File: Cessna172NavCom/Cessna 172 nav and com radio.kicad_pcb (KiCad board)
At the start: 2 copper layers, 180 x 48 mm, 54 parts, among them J1 Conn_02x10_Odd_Even, J2 USB_B_Micro, J3 EN11-HSM1BF20, J4 EN11-HSM1BF20, J5 EN11-HSM1BF20, J6 Conn_01x05, SW1 SW_Push, SW2 SW_Push, SW3 SW_Push, U1 MAX7219 COM standby, U2 3651A, U3 MAX7219 COM standby, U4 3651A, U5 MAX7219 COM standby, U6 3651A, U7 MAX7219 COM standby, U8 3651A

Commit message: Updated trace width for +5V and GND
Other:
- net class +5V: trace_width 1.016 -> 0.4
- net class GND: trace_width 1.016 -> 0.4

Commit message: Mostly laid out
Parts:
- added C12: 0.1uF, Capacitor_SMD:C_0805_2012Metric_Pad1.15x1.40mm_HandSolder, F.Cu at (195.0, 177.0)
- added C13: 0.1uF, Capacitor_SMD:C_0805_2012Metric_Pad1.15x1.40mm_HandSolder, F.Cu at (210.0, 172.0)
- added C14: 0.1uF, Capacitor_SMD:C_0805_2012Metric_Pad1.15x1.40mm_HandSolder, F.Cu at (205.0, 177.0)
- added C15: 0.1uF, Capacitor_SMD:C_0805_2012Metric_Pad1.15x1.40mm_HandSolder, F.Cu at (210.0, 168.0)
- added C16: 0.1uf, Capacitor_SMD:C_0805_2012Metric_Pad1.15x1.40mm_HandSolder, B.Cu at (113.0, 121.0)
- added C17: 0.1uf, Capacitor_SMD:C_0805_2012Metric_Pad1.15x1.40mm_HandSolder, B.Cu at (113.0, 101.0)
- added C18: 0.1uf, Capacitor_SMD:C_0805_2012Metric_Pad1.15x1.40mm_HandSolder, B.Cu at (193.0, 121.0)
- added C19: 0.1uf, Capacitor_SMD:C_0805_2012Metric_Pad1.15x1.40mm_HandSolder, B.Cu at (193.0, 101.0)
- added C20: 0.1uf, Capacitor_SMD:C_0805_2012Metric_Pad1.15x1.40mm_HandSolder, B.Cu at (55.0, 125.0)
- added C21: 0.1uf, Capacitor_SMD:C_0805_2012Metric_Pad1.15x1.40mm_HandSolder, B.Cu at (60.0, 104.0)
- added D5: LED, LED_THT:LED_D5.0mm, F.Cu at (203.0, 171.0)
- added D6: LED, LED_THT:LED_D5.0mm, F.Cu at (195.0, 171.0)
- added D7: LED, LED_THT:LED_D5.0mm, F.Cu at (206.0, 163.0)
- added J7: EN11-HSM1BF20, SamacSys_Parts:EN11HSM1BF20, F.Cu at (60.0, 117.0)
- added J8: Conn_02x20_Odd_Even, SamacSys_Parts:SAMTEC-TST-120-01-X-D, B.Cu at (203.0, 77.5)
- added R18: 220k, Resistor_SMD:R_0805_2012Metric_Pad1.15x1.40mm_HandSolder, F.Cu at (213.0, 164.0)
- added R19: 220k, Resistor_SMD:R_0805_2012Metric_Pad1.15x1.40mm_HandSolder, F.Cu at (200.0, 177.0)
- added R20: 220k, Resistor_SMD:R_0805_2012Metric_Pad1.15x1.40mm_HandSolder, F.Cu at (213.0, 161.0)
- added R21: 10k, Resistor_SMD:R_0805_2012Metric_Pad1.15x1.40mm_HandSolder, B.Cu at (108.0, 121.0)
- added R22: 10k, Resistor_SMD:R_0805_2012Metric_Pad1.15x1.40mm_HandSolder, B.Cu at (108.0, 101.0)
- added R23: 10k, Resistor_SMD:R_0805_2012Metric_Pad1.15x1.40mm_HandSolder, B.Cu at (113.0, 117.0)
- added R24: 10k, Resistor_SMD:R_0805_2012Metric_Pad1.15x1.40mm_HandSolder, B.Cu at (113.0, 105.0)
- added R25: 10k, Resistor_SMD:R_0805_2012Metric_Pad1.15x1.40mm_HandSolder, B.Cu at (188.0, 121.0)
- added R26: 10k, Resistor_SMD:R_0805_2012Metric_Pad1.15x1.40mm_HandSolder, B.Cu at (188.0, 101.0)
- added R27: 10k, Resistor_SMD:R_0805_2012Metric_Pad1.15x1.40mm_HandSolder, B.Cu at (193.0, 117.0)
- added R28: 10k, Resistor_SMD:R_0805_2012Metric_Pad1.15x1.40mm_HandSolder, B.Cu at (193.0, 105.0)
- added R29: 10k, Resistor_SMD:R_0805_2012Metric_Pad1.15x1.40mm_HandSolder, B.Cu at (60.0, 125.0)
- added R30: 10k, Resistor_SMD:R_0805_2012Metric_Pad1.15x1.40mm_HandSolder, B.Cu at (55.0, 104.0)
- added R31: 10k, Resistor_SMD:R_0805_2012Metric_Pad1.15x1.40mm_HandSolder, B.Cu at (60.0, 121.0)
- added R32: 10k, Resistor_SMD:R_0805_2012Metric_Pad1.15x1.40mm_HandSolder, B.Cu at (60.0, 108.0)
- added SW4: SW_Push, Button_Switch_THT:SW_PUSH_6mm_H8mm, F.Cu at (184.0, 161.0)
- added SW5: SW_Push, Button_Switch_THT:SW_PUSH_6mm_H8mm, F.Cu at (184.0, 169.0)
- added SW6: SW_Push, Button_Switch_THT:SW_PUSH_6mm_H8mm, F.Cu at (195.0, 161.0)
- added U10: 3651A, Cessna 172 nav and com radio:3651A, F.Cu at (61.0, 91.0)
- added U11: MAX7219 COM standby, Package_SO:SSOP-24_3.9x8.7mm_P0.635mm, B.Cu at (140.0, 91.0)
- added U12: 3651A, Cessna 172 nav and com radio:3651A, F.Cu at (140.0, 91.0)
- added U13: MAX7219 COM standby, Package_SO:SSOP-24_3.9x8.7mm_P0.635mm, B.Cu at (178.0, 91.0)
- added U14: 3651A, Cessna 172 nav and com radio:3651A, F.Cu at (178.0, 91.0)
- added U15: MAX7219 COM standby, Package_SO:SSOP-24_3.9x8.7mm_P0.635mm, B.Cu at (99.0, 91.0)
- added U16: 3651A, Cessna 172 nav and com radio:3651A, F.Cu at (99.0, 91.0)
- added U9: MAX7219 COM standby, Package_SO:SSOP-24_3.9x8.7mm_P0.635mm, B.Cu at (61.0, 91.0)
- J1: value Conn_02x10_Odd_Even -> EN11-HSM1BF20; footprint Connector_PinHeader_2.54mm:PinHeader_2x10_P2.54mm_Vertical -> SamacSys_Parts:EN11HSM1BF20; moved to F.Cu
- J6: value Conn_01x05 -> EN11-HSM1BF20; footprint Connector_PinHeader_2.54mm:PinHeader_1x05_P2.54mm_Vertical -> SamacSys_Parts:EN11HSM1BF20
- moved J6 65.1 mm to (193.0, 113.0), turned to 90 degrees
- moved J1 56.2 mm to (113.5, 113.0), turned to 90 degrees
- moved C1 55.0 mm to (35.0, 101.0)
- moved D1 55.0 mm to (32.0, 96.0)
- moved J2 55.0 mm to (32.8, 109.0)
- moved R2 55.0 mm to (36.0, 96.0)
- moved H2 47.0 mm to (35.0, 120.0)
- moved H4 47.0 mm to (205.0, 120.0)
- moved R1 23.3 mm to (141.0, 56.0)
- moved RV1 23.3 mm to (146.0, 56.0)
- moved D3 4.00 mm to (138.0, 66.0)
- moved R4 4.00 mm to (144.0, 66.0)
- moved SW3 4.00 mm to (125.0, 64.0)
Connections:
- C1 pad 2: GND -> +5V
- C10 pad 1: GND -> +5V
- C11 pad 2: GND -> +5V
- C2 pad 2: GND -> +5V
- C3 pad 2: GND -> +5V
- C4 pad 2: GND -> +5V
- C5 pad 2: GND -> +5V
- C6 pad 1: GND -> +5V
- C7 pad 2: GND -> +5V
- C8 pad 1: GND -> +5V
- C9 pad 2: GND -> +5V
- D1 pad 1: GND -> +5V
- D2 pad 1: GND -> +5V
- D3 pad 1: GND -> +5V
- D4 pad 1: GND -> +5V
- J2 pad 5: GND -> +5V
- J3 pad C1: GND -> +5V
- J3 pad D1: COMM_KHZ_SW -> COMM1_KHZ_SW
- J3 pad E1: GND -> +5V
- J4 pad C1: GND -> +5V
- J4 pad D1: NAV_KHZ_SW -> NAV1_KHZ_SW
- J4 pad E1: GND -> +5V
- J5 pad C1: GND -> +5V
- J5 pad D1: TEST_SW -> TEST1_SW
- J5 pad E1: GND -> +5V
- R11 pad 1: NAV_LEFT -> NAV1_LEFT
- R12 pad 2: NAV_RIGHT -> NAV1_RIGHT
- R15 pad 1: COMM_VOL_LEFT -> COMM1_VOL_LEFT
- R16 pad 2: COMM_VOL_RIGHT -> COMM1_VOL_RIGHT
- R17 pad 2: CHAN_LED -> CHAN1_LED
- R2 pad 1: Net-(D1-Pad2) -> +5V
- R2 pad 2: +5V -> Net-(D1-Pad2)
- R3 pad 2: TEST_LED -> TEST1_LED
- R4 pad 2: IDENT_LED -> IDENT1_LED
- R7 pad 1: COMM_LEFT -> COMM1_LEFT
- R8 pad 2: COMM_RIGHT -> COMM1_RIGHT
- SW1 pad 1: GND -> +5V
- SW1 pad 2: COMM_TX_SW -> COMM1_TX_SW
- SW2 pad 1: GND -> +5V
- SW2 pad 2: NAV_TX_SW -> NAV1_TX_SW
- SW3 pad 1: GND -> +5V
- SW3 pad 2: IDENT_SW -> IDENT1_SW
- U1 pad 4: GND -> +5V
- U1 pad 9: GND -> +5V
- U3 pad 4: GND -> +5V
- U3 pad 9: GND -> +5V
- U5 pad 4: GND -> +5V
- U5 pad 9: GND -> +5V
- U7 pad 24: DOUT -> /sheet5F68A9C2/DIN
- U7 pad 4: GND -> +5V
- U7 pad 9: GND -> +5V
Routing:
- removed copper zone on B.Cu, net (none)
- removed copper zone on F.Cu, net (none)
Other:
- board size 180 x 48 mm -> 180 x 95 mm
- board text added: "COMM1 active"
- board text added: "COMM1 standby"
- board text added: "COMM1 tuner"
- board text added: "COMM1 volume"
- board text added: "COMM2 active"
- board text added: "COMM2 standby"
- board text added: "COMM2 tuning"
- board text added: "COMM2 volume"
- board text added: "NAV1 active"
- board text added: "NAV1 standby"
- board text added: "NAV1 tuner"
- board text added: "NAV2 active"
- board text added: "NAV2 standby"
- board text added: "NAV2 tuning"
- board text removed: "COMM active"
- board text removed: "COMM standby"
- board text removed: "COMM tuner"
- board text removed: "COMM volume"
- board text removed: "NAV active"
- board text removed: "NAV standby"
- board text removed: "NAV tuner"

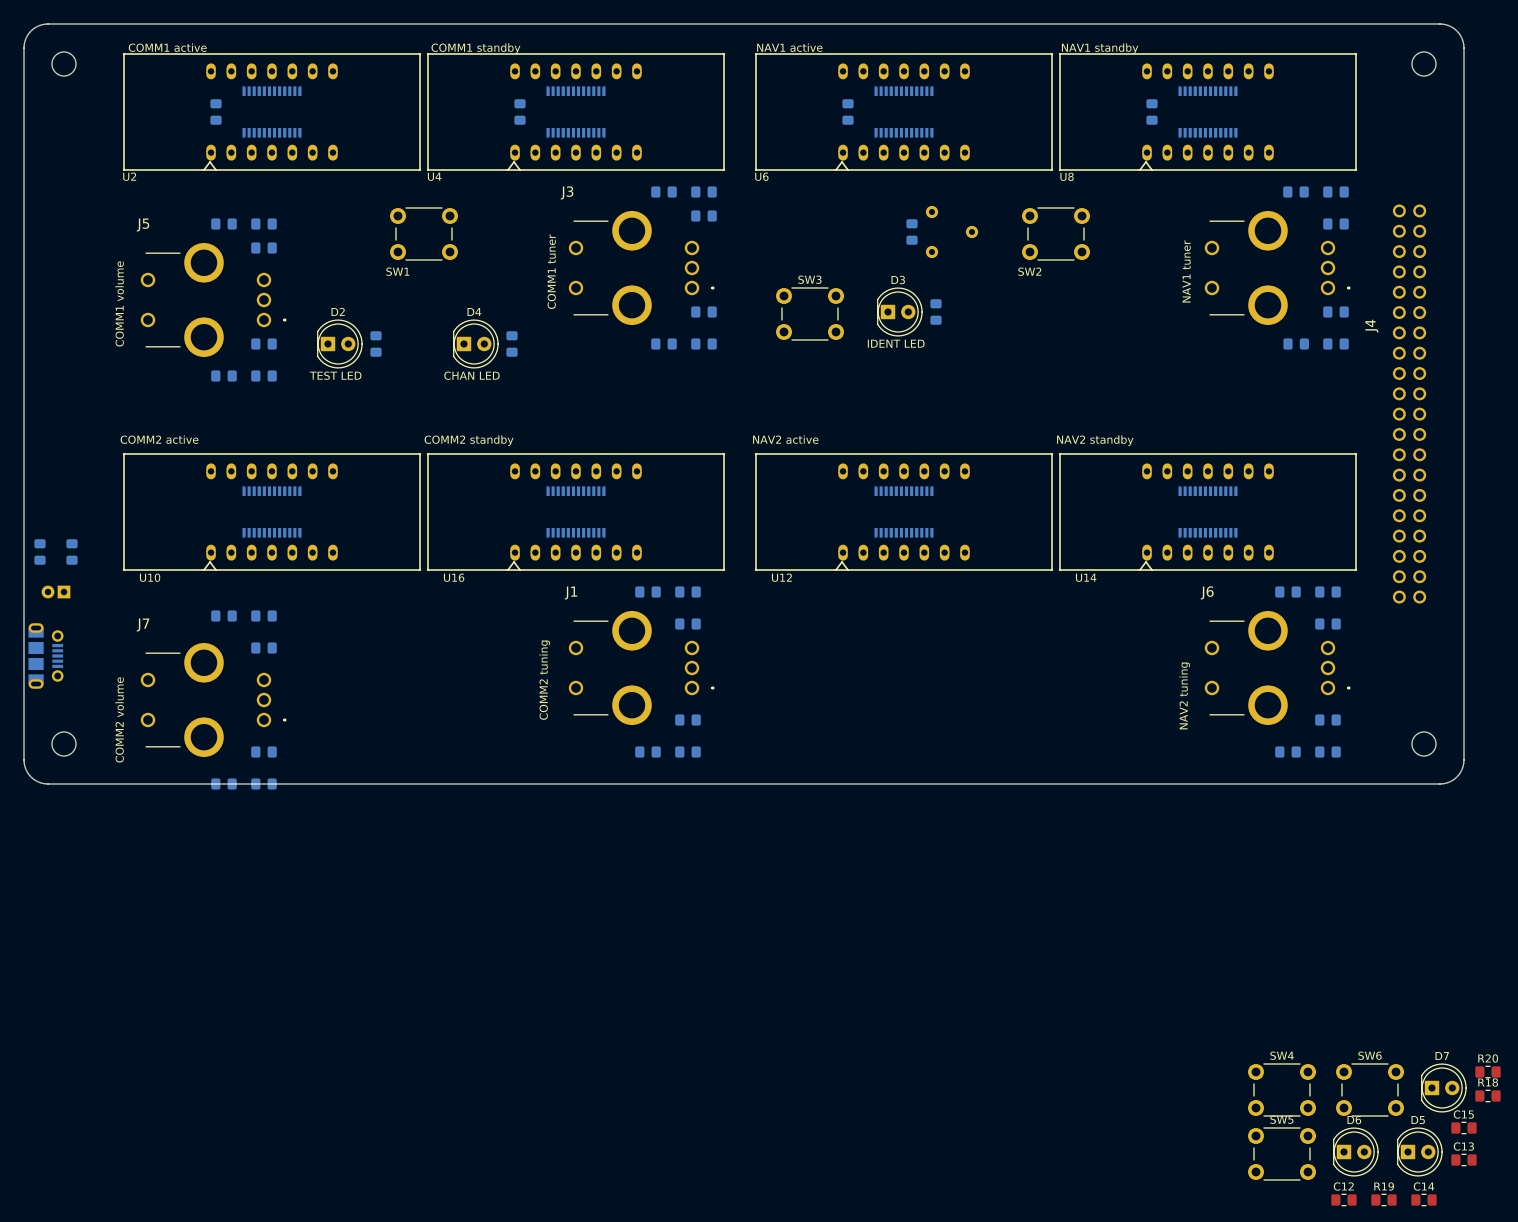
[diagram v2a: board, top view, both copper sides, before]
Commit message: Full 2up layout done
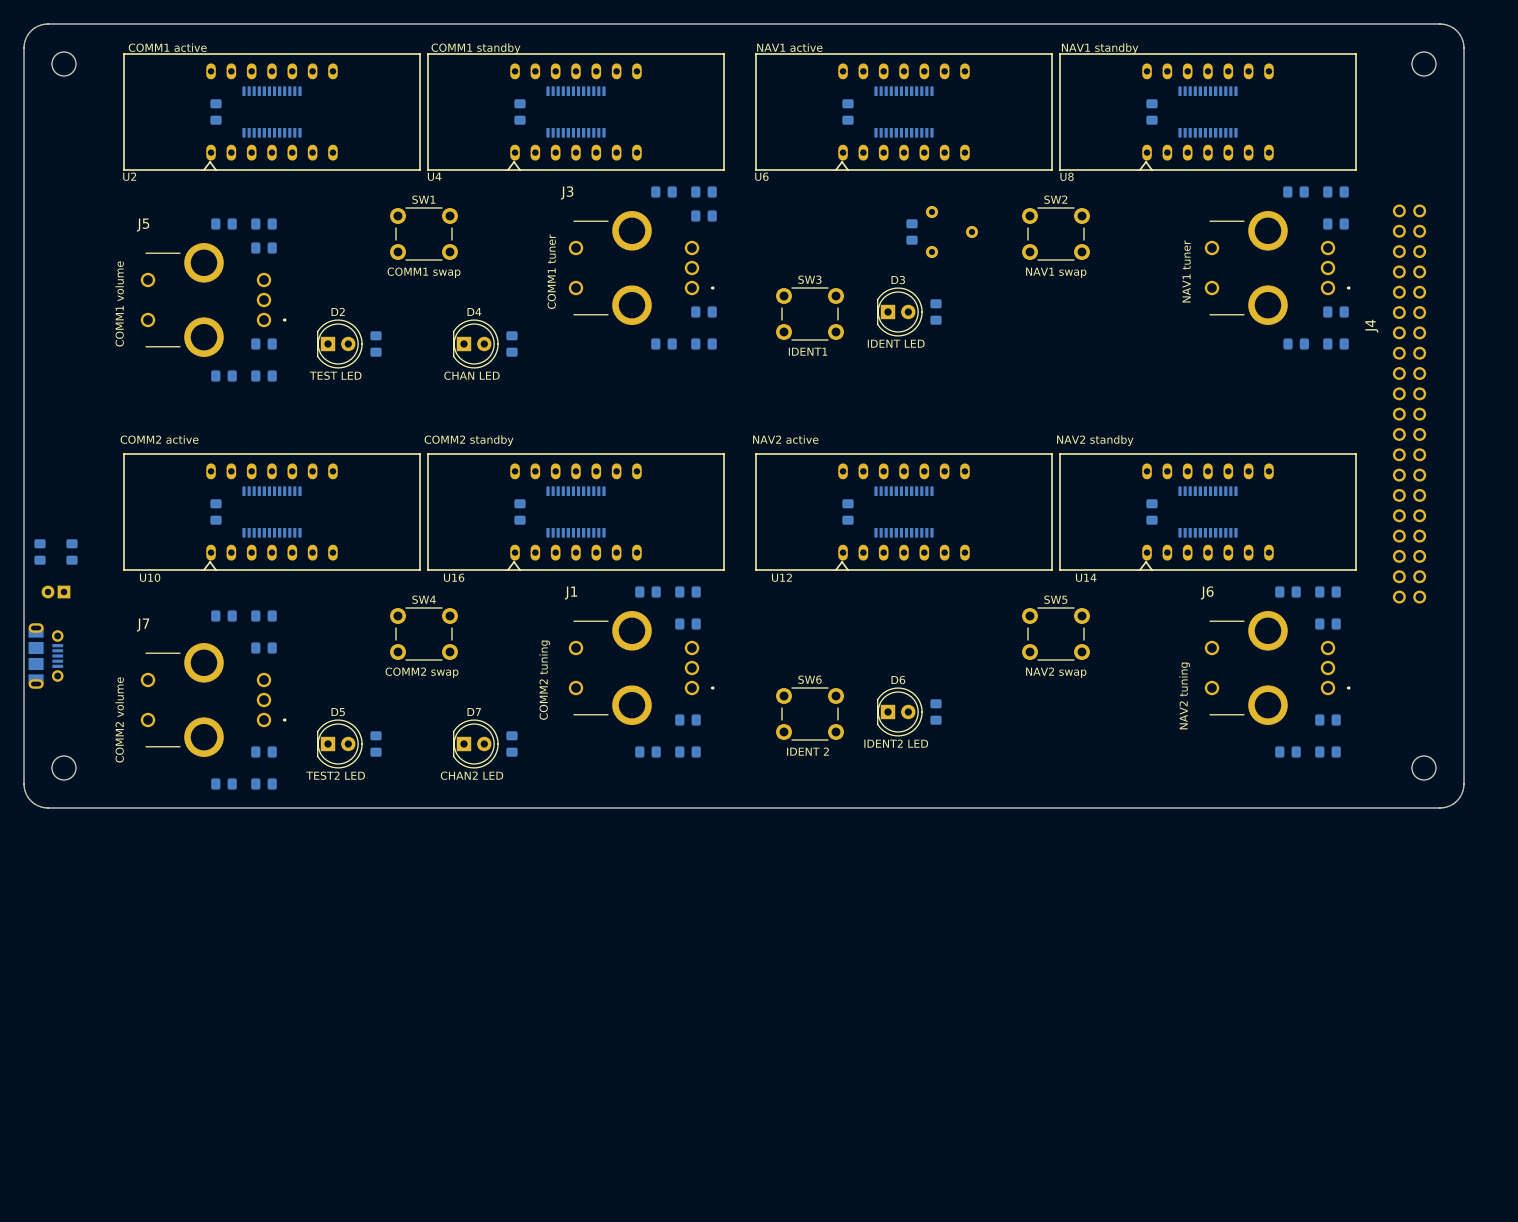
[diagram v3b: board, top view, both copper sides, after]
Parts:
- C12, C13, C14, C15, R18, R19, R20: moved to B.Cu
- moved C12 165.2 mm to (54.0, 91.0), turned to 270 degrees
- moved R18 145.8 mm to (74.0, 120.0), turned to 90 degrees
- moved D5 144.3 mm to (68.0, 120.0)
- moved C13 143.1 mm to (92.0, 91.0), turned to 270 degrees
- moved R20 128.7 mm to (91.0, 120.0), turned to 90 degrees
- moved D7 128.4 mm to (85.0, 120.0)
- moved SW4 121.5 mm to (76.8, 104.0)
- moved C14 112.2 mm to (133.0, 91.0), turned to 270 degrees
- moved C15 86.3 mm to (171.0, 91.0), turned to 270 degrees
- moved SW6 84.3 mm to (125.0, 114.0)
- moved R19 82.8 mm to (144.0, 116.0), turned to 90 degrees
- moved D6 79.2 mm to (138.0, 116.0)
- moved SW5 70.9 mm to (155.8, 104.0)
- moved H2 3.00 mm to (35.0, 123.0)
- moved H4 3.00 mm to (205.0, 123.0)
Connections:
- C1 pad 2: +5V -> GND
- C10 pad 1: +5V -> GND
- C11 pad 2: +5V -> GND
- C12 pad 2: +5V -> GND
- C13 pad 2: +5V -> GND
- C14 pad 2: +5V -> GND
- C15 pad 2: +5V -> GND
- C16 pad 1: +5V -> GND
- C17 pad 2: +5V -> GND
- C18 pad 1: +5V -> GND
- C19 pad 2: +5V -> GND
- C2 pad 2: +5V -> GND
- C20 pad 1: +5V -> GND
- C21 pad 2: +5V -> GND
- C3 pad 2: +5V -> GND
- C4 pad 2: +5V -> GND
- C5 pad 2: +5V -> GND
- C6 pad 1: +5V -> GND
- C7 pad 2: +5V -> GND
- C8 pad 1: +5V -> GND
- C9 pad 2: +5V -> GND
- D1 pad 1: +5V -> GND
- D2 pad 1: +5V -> GND
- D3 pad 1: +5V -> GND
- D4 pad 1: +5V -> GND
- D5 pad 1: +5V -> GND
- D6 pad 1: +5V -> GND
- D7 pad 1: +5V -> GND
- J1 pad C1: +5V -> GND
- J1 pad E1: +5V -> GND
- J2 pad 5: +5V -> GND
- J3 pad C1: +5V -> GND
- J3 pad E1: +5V -> GND
- J4 pad C1: +5V -> GND
- J4 pad E1: +5V -> GND
- J5 pad C1: +5V -> GND
- J5 pad E1: +5V -> GND
- J6 pad C1: +5V -> GND
- J6 pad E1: +5V -> GND
- J7 pad C1: +5V -> GND
- J7 pad E1: +5V -> GND
- SW1 pad 1: +5V -> GND
- SW2 pad 1: +5V -> GND
- SW3 pad 1: +5V -> GND
- SW4 pad 1: +5V -> GND
- SW5 pad 1: +5V -> GND
- SW6 pad 1: +5V -> GND
- U1 pad 4: +5V -> GND
- U1 pad 9: +5V -> GND
- U11 pad 4: +5V -> GND
- U11 pad 9: +5V -> GND
- U13 pad 4: +5V -> GND
- U13 pad 9: +5V -> GND
- U15 pad 4: +5V -> GND
- U15 pad 9: +5V -> GND
- U3 pad 4: +5V -> GND
- U3 pad 9: +5V -> GND
- U5 pad 4: +5V -> GND
- U5 pad 9: +5V -> GND
- U7 pad 4: +5V -> GND
- U7 pad 9: +5V -> GND
- U9 pad 4: +5V -> GND
- U9 pad 9: +5V -> GND
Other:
- board size 180 x 95 mm -> 180 x 98 mm
- board text added: "CHAN2 LED"
- board text added: "COMM1 swap"
- board text added: "COMM2 swap"
- board text added: "IDENT 2"
- board text added: "IDENT1"
- board text added: "IDENT2 LED"
- board text added: "NAV1 swap"
- board text added: "NAV2 swap"
- board text added: "TEST2 LED"

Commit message: Merge connector mapping
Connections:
- C12 pad 1: +5V -> Net-(C12-Pad1)
- C12 pad 2: GND -> Net-(C12-Pad2)
- C13 pad 1: +5V -> Net-(C12-Pad1)
- C13 pad 2: GND -> Net-(C12-Pad2)
- C14 pad 1: +5V -> Net-(C12-Pad1)
- C14 pad 2: GND -> Net-(C12-Pad2)
- C15 pad 1: +5V -> Net-(C12-Pad1)
- C15 pad 2: GND -> Net-(C12-Pad2)
- C2 pad 1: +5V -> Net-(C12-Pad1)
- C2 pad 2: GND -> Net-(C12-Pad2)
- C3 pad 1: +5V -> Net-(C12-Pad1)
- C3 pad 2: GND -> Net-(C12-Pad2)
- C4 pad 1: +5V -> Net-(C12-Pad1)
- C4 pad 2: GND -> Net-(C12-Pad2)
- C5 pad 1: +5V -> Net-(C12-Pad1)
- C5 pad 2: GND -> Net-(C12-Pad2)
- J8 pad 1: Net-(J8-Pad1) -> LOAD
- J8 pad 10: Net-(J8-Pad10) -> COMM2_RIGHT
- J8 pad 11: Net-(J8-Pad11) -> COMM1_KHZ_SW
- J8 pad 12: Net-(J8-Pad12) -> COMM2_KHZ_SW
- J8 pad 13: Net-(J8-Pad13) -> COMM1_TX_SW
- J8 pad 14: Net-(J8-Pad14) -> COMM2_TX_SW
- J8 pad 15: Net-(J8-Pad15) -> NAV1_LEFT
- J8 pad 16: Net-(J8-Pad16) -> NAV2_LEFT
- J8 pad 17: Net-(J8-Pad17) -> NAV1_RIGHT
- J8 pad 18: Net-(J8-Pad18) -> NAV2_RIGHT
- J8 pad 19: Net-(J8-Pad19) -> NAV1_KHZ_SW
- J8 pad 2: Net-(J8-Pad2) -> +5V
- J8 pad 20: Net-(J8-Pad20) -> NAV2_KHZ_SW
- J8 pad 21: Net-(J8-Pad21) -> NAV1_TX_SW
- J8 pad 22: Net-(J8-Pad22) -> NAV2_TX_SW
- J8 pad 23: Net-(J8-Pad23) -> COMM1_VOL_LEFT
- J8 pad 24: Net-(J8-Pad24) -> COMM2_VOL_LEFT
- J8 pad 25: Net-(J8-Pad25) -> COMM1_VOL_RIGHT
- J8 pad 26: Net-(J8-Pad26) -> COMM2_VOL_RIGHT
- J8 pad 27: Net-(J8-Pad27) -> TEST1_SW
- J8 pad 28: Net-(J8-Pad28) -> TEST2_SW
- J8 pad 29: Net-(J8-Pad29) -> TEST1_LED
- J8 pad 3: Net-(J8-Pad3) -> CLK
- J8 pad 30: Net-(J8-Pad30) -> TEST2_LED
- J8 pad 31: Net-(J8-Pad31) -> IDENT1_SW
- J8 pad 32: Net-(J8-Pad32) -> IDENT2_SW
- J8 pad 33: Net-(J8-Pad33) -> IDENT1_LED
- J8 pad 34: Net-(J8-Pad34) -> IDENT2_LED
- J8 pad 35: Net-(J8-Pad35) -> CHAN1_LED
- J8 pad 36: Net-(J8-Pad36) -> CHAN2_LED
- J8 pad 4: Net-(J8-Pad4) -> GND
- J8 pad 5: Net-(J8-Pad5) -> DIN
- J8 pad 7: Net-(J8-Pad7) -> COMM1_LEFT
- J8 pad 8: Net-(J8-Pad8) -> COMM2_LEFT
- J8 pad 9: Net-(J8-Pad9) -> COMM1_RIGHT
